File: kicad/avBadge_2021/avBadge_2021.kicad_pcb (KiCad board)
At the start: 2 copper layers, 115 x 75 mm, 36 parts, among them J1 AVR-ISP-6, Q1 2N3904, SW1 SW_Push_Dual, SW2 SW_SPDT, U1 ATtiny84A-SSU

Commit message: arduino code updates and manufactured v01 gerbers completed.
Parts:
- Q1: footprint TO_SOT_Packages_SMD:SOT-23 -> aerospace_badge:SOT-23-NPN

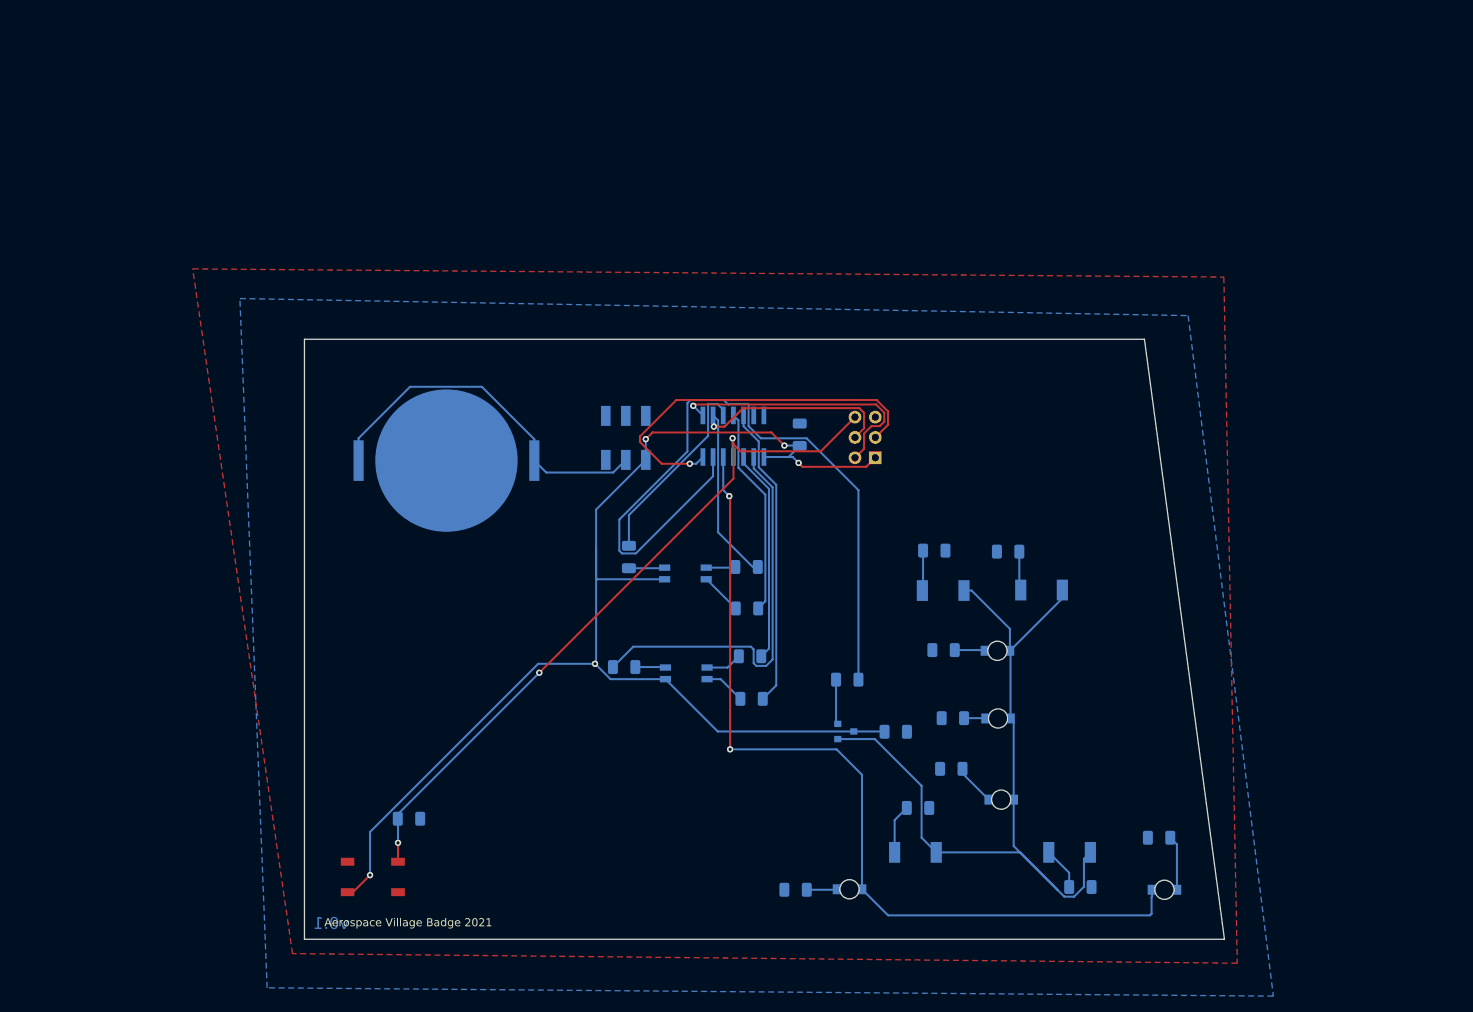
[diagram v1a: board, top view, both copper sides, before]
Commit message: refactor of kicad files working through incorporation of art and new MCU design.
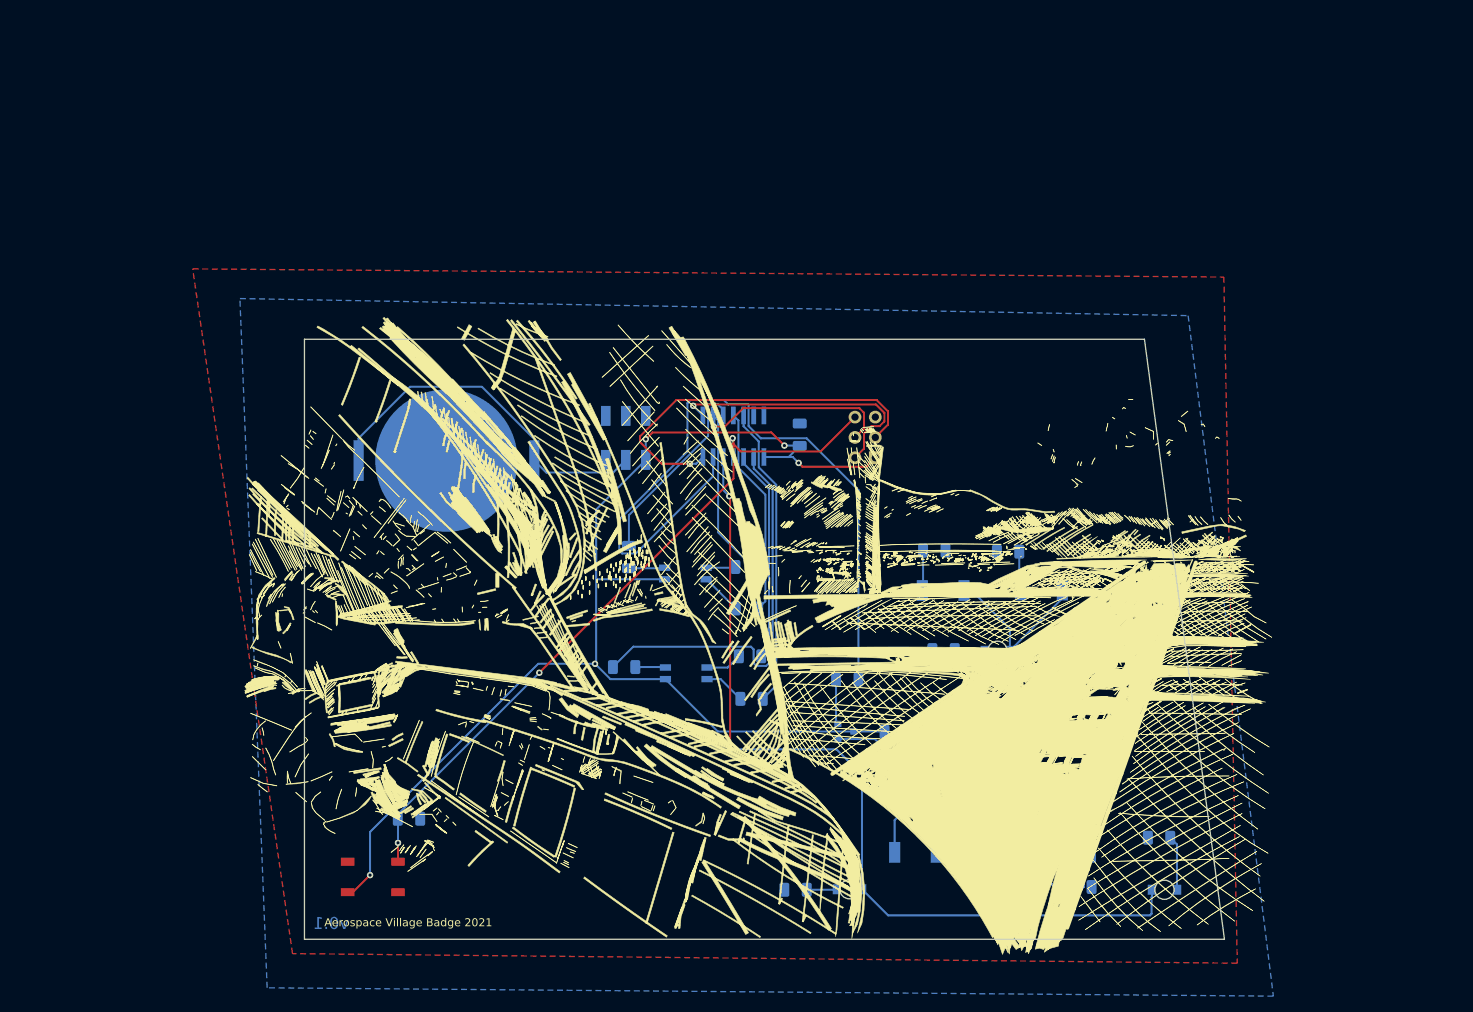
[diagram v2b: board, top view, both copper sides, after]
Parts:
- added svg2mod: G***, aerospace_badge:test, F.Cu at (142.1, 102.9)

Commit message: v0.2 gerber builtout and sent for fabrication.
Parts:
- removed the D5 at (171.4, 134.1)
- removed the SW1 at (103.5, 137.2)
- removed svg2mod: G***, aerospace_badge:test
- added D12: LED, sunled:XZMYK45WT-9, B.Cu at (185.3, 117.4)
- added D4: LED, sunled:XZDGK45WT-9, B.Cu at (205.2, 81.1)
- added P1: SerialConnector, aerospace_badge:serialConnector, B.Cu at (116.6, 114.2)
- added R11: 330, Resistors_SMD:R_1206_3216Metric, B.Cu at (198.5, 81.1)
- added R12: 10K, Resistors_SMD:R_1206_3216Metric, B.Cu at (137.5, 125.0)
- added R7: 10K, Resistors_SMD:R_1206_3216Metric, B.Cu at (129.1, 120.2)
- added S1: OpenConnections, aerospace_badge:artboard, F.Cu at (150.5, 104.7)
- added VR1: TLV702, TO_SOT_Packages_SMD:SOT-23-5, B.Cu at (110.0, 95.4)
- BT1: footprint Battery:BatteryHolder_Keystone_3034_1x20mm -> aerospace_badge:BHX2-2032
- D1, D2: value APFA3010 -> SunLED_RGB_ReverseMount
- D10, D11: footprint aerospace_badge:led_in-s124ar -> sunled:XZMYK45WT-9
- D6: footprint sunled:XZDGK45WT-9 -> sunled:XZM2CRK45WT-9
- D8: footprint sunled:XZM2CRK45WT-9 -> sunled:XZDGK45WT-9
- D9: footprint aerospace_badge:led_in-s124ar -> sunled:XZDGK45WT-9
- J1: moved to F.Cu
- U1: value ATtiny84A-SSU -> ATmega8-16AU; footprint aerospace_badge:attiny84 -> digikey-footprints:TQFP-32_7x7mm
- moved J1 68.6 mm to (95.2, 86.9), turned to 45 degrees
- moved C1 47.7 mm to (113.6, 101.9)
- moved D1 40.1 mm to (165.4, 78.7)
- moved R2 35.1 mm to (172.6, 87.3)
- moved R4 34.6 mm to (157.0, 84.3)
- moved U1 33.5 mm to (124.3, 105.2), turned to 0 degrees
- moved R6 33.4 mm to (172.6, 84.3)
- moved R1 32.2 mm to (172.5, 80.4)
- moved R5 30.4 mm to (172.2, 77.4)
- moved R3 29.3 mm to (157.6, 77.9), turned to 0 degrees
- moved D7 29.1 mm to (188.9, 126.8)
- moved R9 28.8 mm to (135.1, 120.1)
- moved D11 28.4 mm to (197.3, 103.5), turned to 180 degrees
- moved D9 27.6 mm to (206.4, 96.8), turned to 270 degrees
- moved R19 27.3 mm to (201.6, 107.6), turned to 0 degrees
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- renumbered D4 to D5, R2 to R1, R8 to R10, R10 to R13, R11 to R14, R12 to R15, R13 to R16, R14 to R17, R15 to R18, R16 to R19, R1 to R2, R17 to R20, R4 to R3, R3 to R4, R6 to R5, R5 to R6, R7 to R8, SW2 to SW1
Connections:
- R1 pad 1: Net-(R2-Pad1) -> Net-(R1-Pad1)
- R1 pad 2: Net-(D2-Pad1) -> Net-(D1-Pad1)
- R13 pad 2: Net-(R10-Pad2) -> Net-(R13-Pad2)
- R14 pad 1: Net-(D5-Pad1) (its old number) -> Net-(D6-Pad1)
- R15 pad 1: Net-(D6-Pad1) -> Net-(D7-Pad1)
- R16 pad 1: Net-(D7-Pad1) -> Net-(D8-Pad1)
- R17 pad 1: Net-(D8-Pad1) -> Net-(D9-Pad1)
- R18 pad 1: Net-(D9-Pad1) -> Net-(D10-Pad1)
- R19 pad 1: Net-(D10-Pad1) -> Net-(D11-Pad1)
- R2 pad 1: Net-(R1-Pad1) -> Net-(R2-Pad1)
- R2 pad 2: Net-(D1-Pad1) -> Net-(D2-Pad1)
- R20 pad 1: Net-(D11-Pad1) -> Net-(D12-Pad1)
- R3 pad 1: Net-(R4-Pad1) -> Net-(R3-Pad1)
- R3 pad 2: Net-(D2-Pad3) -> Net-(D1-Pad3)
- R4 pad 1: Net-(R3-Pad1) -> Net-(R4-Pad1)
- R4 pad 2: Net-(D1-Pad3) -> Net-(D2-Pad3)
- R5 pad 1: Net-(J1-Pad3) -> Net-(R5-Pad1)
- R5 pad 2: Net-(D2-Pad4) -> Net-(D1-Pad4)
- R6 pad 1: Net-(R5-Pad1) -> Net-(R6-Pad1)
- R6 pad 2: Net-(D1-Pad4) -> Net-(D2-Pad4)
- R9 pad 2: Net-(J1-Pad5) -> Net-(R9-Pad2)
- SW1 pad 1: VCC -> Net-(SW1-Pad1)
- U1 pad 1: VCC -> Net-(R12-Pad2)
- U1 pad 11: Net-(R2-Pad1) -> Net-(U1-Pad11)
- U1 pad 12: Net-(R1-Pad1) -> Net-(D4-Pad2)
- U1 pad 13: Net-(U1-Pad13) -> Net-(R6-Pad1)
- U1 pad 14: GND -> Net-(R13-Pad2)
- U1 pad 2: Net-(R3-Pad1) -> Net-(R7-Pad2)
- U1 pad 3: Net-(R5-Pad1) -> GND
- U1 pad 4: Net-(J1-Pad5) -> VCC
- U1 pad 5: Net-(D3-Pad2) -> GND
- U1 pad 6: Net-(R10-Pad2) -> VCC
- U1 pad 7: Net-(J1-Pad4) -> Net-(U1-Pad7)
- U1 pad 8: Net-(J1-Pad1) -> Net-(U1-Pad8)
- U1 pad 9: Net-(J1-Pad3) -> Net-(R2-Pad1)
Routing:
- net GND: track 0.00 -> 128.6 mm, vias 0 -> 6
- net Net-(D4-Pad2): track 0.00 -> 95.6 mm, vias 0 -> 2
- net Net-(R10-Pad2): track 91.8 -> 0.00 mm
- net VCC: track 166.1 -> 257.8 mm, vias 5 -> 2
- net Net-(R6-Pad1): track 0.00 -> 85.8 mm, vias 0 -> 2
- net Net-(SW1-Pad1): track 0.00 -> 65.1 mm
- net Net-(R3-Pad1): track 50.4 -> 114.3 mm, vias 0 -> 3
- net Net-(R13-Pad2): track 0.00 -> 53.7 mm, vias 0 -> 2
- net Net-(R5-Pad1): track 26.6 -> 79.2 mm
- net Net-(J1-Pad5): track 90.1 -> 38.3 mm, vias 3 -> 1
- net Net-(R2-Pad1): track 26.2 -> 63.4 mm, vias 0 -> 2
- net Net-(R1-Pad1): track 38.4 -> 73.3 mm
- net Net-(R9-Pad2): track 0.00 -> 34.6 mm, vias 0 -> 2
- net Net-(R12-Pad2): track 0.00 -> 34.2 mm, vias 0 -> 2
- net Net-(R7-Pad2): track 0.00 -> 32.6 mm, vias 0 -> 1
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- added copper zone on F.Cu, net GND
- removed copper zone on F.Cu, net VCC
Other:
- board size 115 x 75 mm -> 127 x 78 mm
- rule pad_to_mask_clearance: 0.05 -> 0
- board text added: "v0.2"
- board text removed: "v0.1"

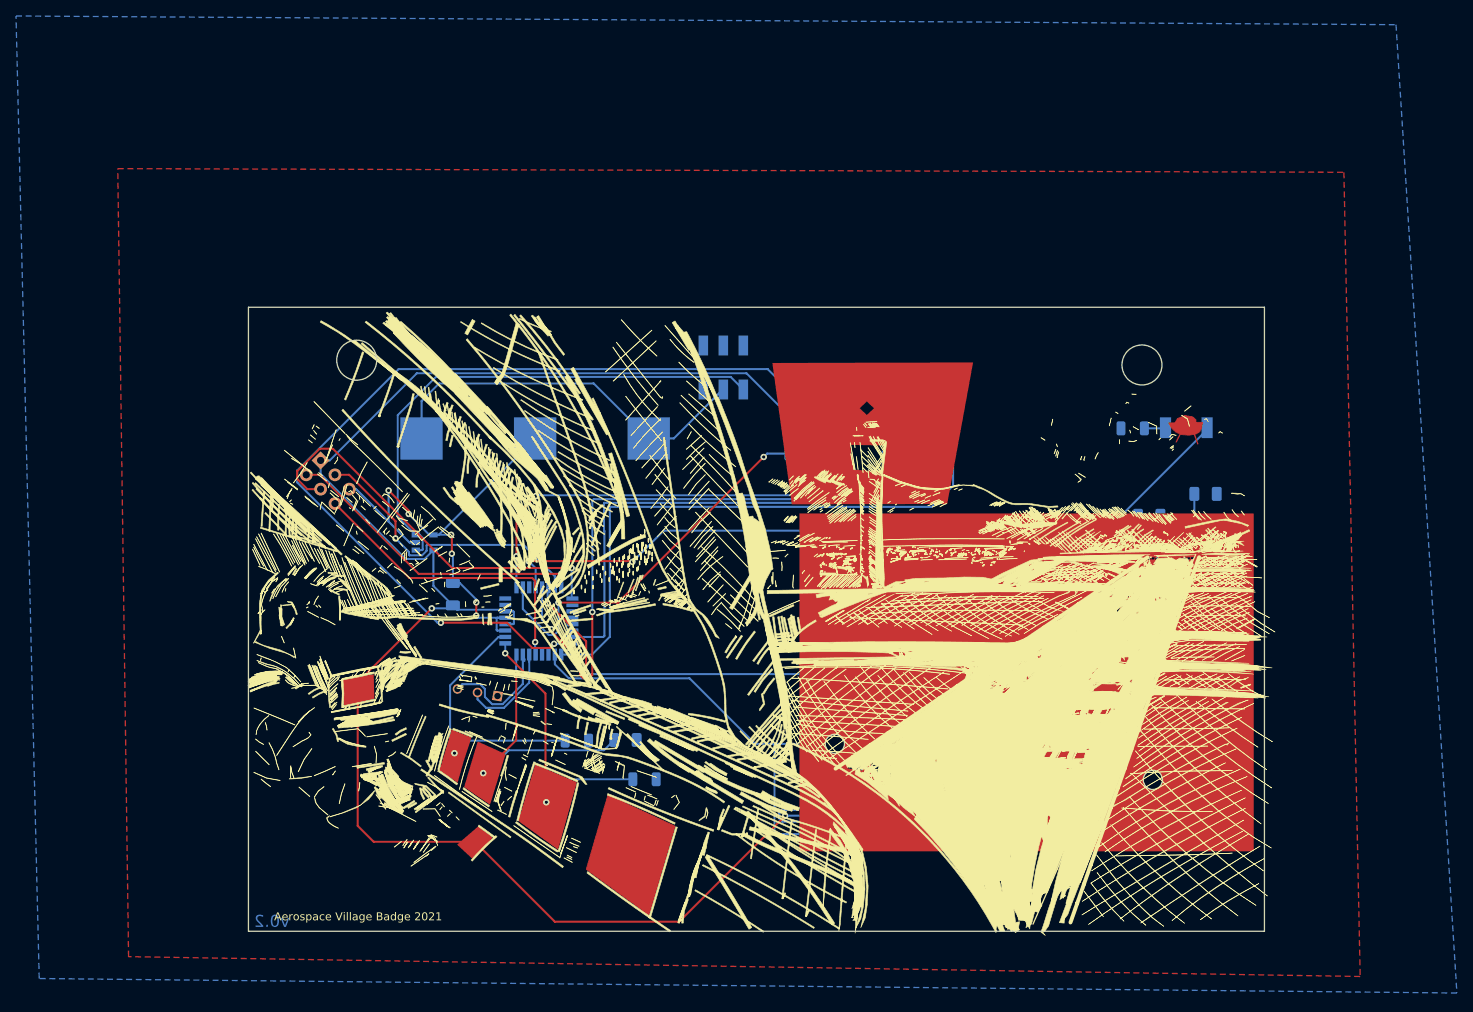
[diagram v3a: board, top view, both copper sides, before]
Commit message: incremental improvements to art, edgecuts, layout
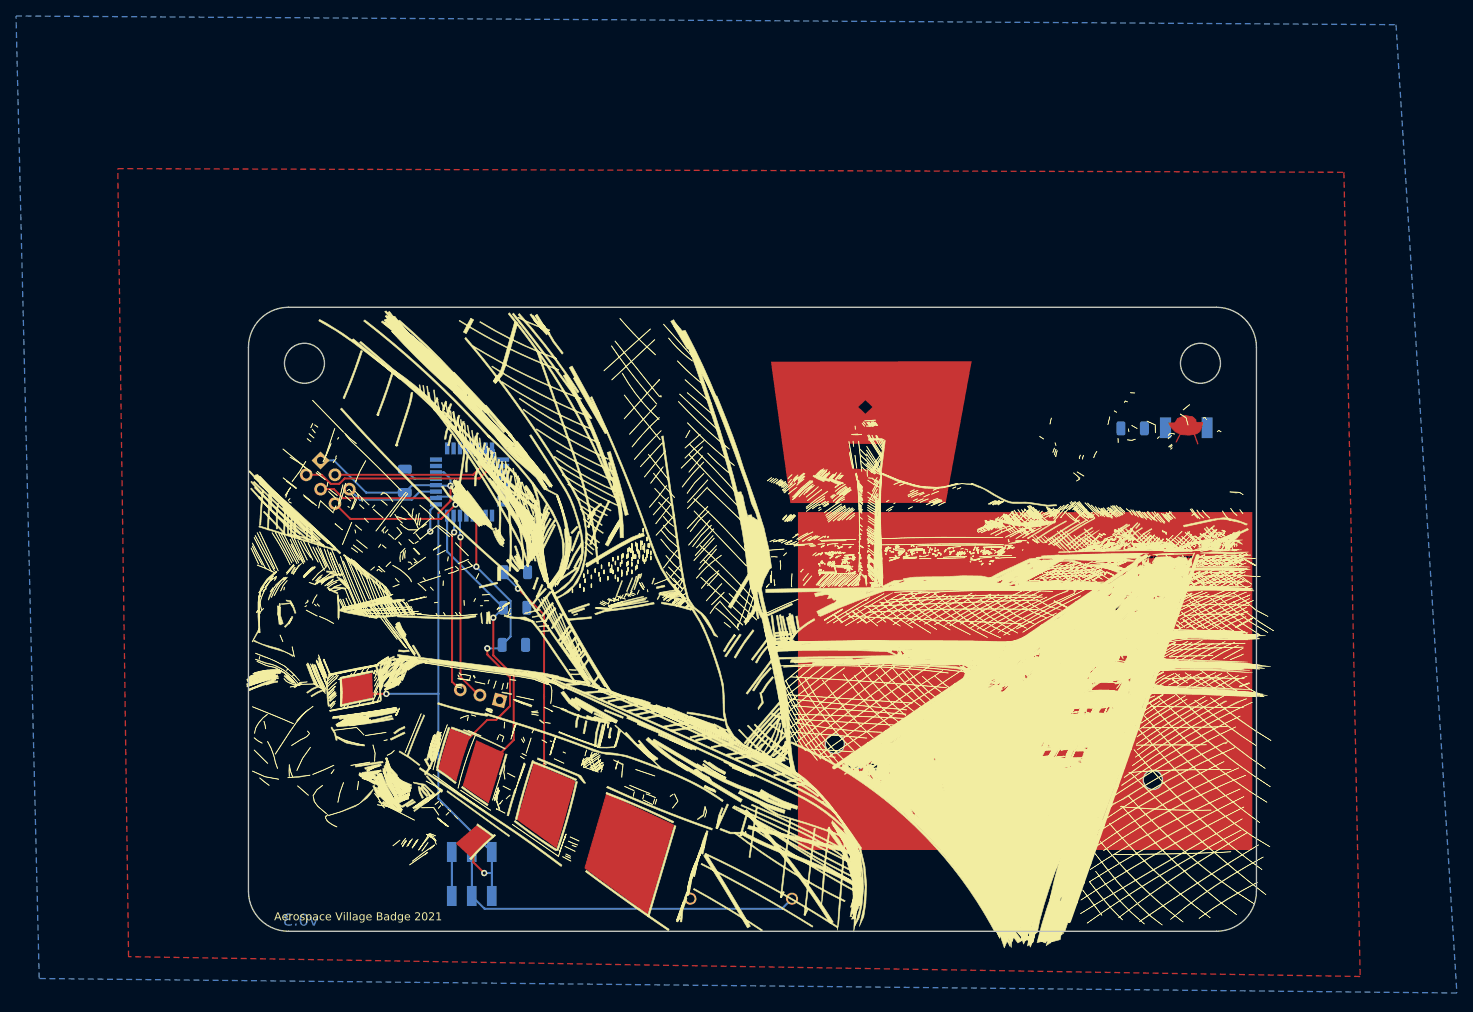
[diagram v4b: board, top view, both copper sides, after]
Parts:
- removed D9: LED, sunled:XZDGK45WT-9
- removed R17: 330, Resistors_SMD:R_1206_3216Metric
- removed VR1: TLV702, TO_SOT_Packages_SMD:SOT-23-5
- BT1: footprint aerospace_badge:BHX2-2032 -> 2479_battery_holder:2479
- moved SW1 70.7 mm to (115.9, 136.8)
- moved BT1 40.4 mm to (144.9, 116.8), turned to 270 degrees
- moved R12 30.5 mm to (121.4, 99.1)
- moved D6 21.7 mm to (189.5, 123.9)
- moved D7 21.7 mm to (167.5, 123.7)
- moved R9 21.5 mm to (121.3, 103.6)
- moved R15 20.3 mm to (167.7, 127.9)
- moved R14 19.5 mm to (182.9, 124.5)
- moved U1 19.4 mm to (115.6, 87.8)
- moved R19 15.9 mm to (187.9, 99.5)
- moved C1 15.4 mm to (107.5, 87.7)
- moved R7 14.3 mm to (121.2, 108.2)
- moved R18 9.83 mm to (186.8, 107.4)
- moved D12 9.12 mm to (193.7, 113.7), turned to 0 degrees
- moved R16 8.29 mm to (192.4, 93.4), turned to 0 degrees
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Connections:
- SW1 pad 1: Net-(SW1-Pad1) -> VCC
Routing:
- net VCC: track 257.8 -> 92.1 mm, vias 2 -> 3
- net Net-(R3-Pad1): track 114.3 -> 0.00 mm, vias 3 -> 0
- net GND: track 128.6 -> 16.2 mm, vias 6 -> 0
- net Net-(D3-Pad2): track 98.7 -> 0.00 mm
- net Net-(D4-Pad2): track 95.6 -> 0.00 mm, vias 2 -> 0
- net Net-(R6-Pad1): track 85.8 -> 0.00 mm, vias 2 -> 0
- net Net-(R5-Pad1): track 79.2 -> 0.00 mm
- net Net-(R1-Pad1): track 73.3 -> 0.00 mm
- net Net-(D10-Pad2): track 71.7 -> 0.00 mm
- net Net-(SW1-Pad1): track 65.1 -> 0.00 mm
- net Net-(R2-Pad1): track 63.4 -> 0.00 mm, vias 2 -> 0
- net Net-(R13-Pad2): track 53.7 -> 0.00 mm, vias 2 -> 0
- net Net-(R4-Pad1): track 49.7 -> 0.00 mm, vias 2 -> 0
- net Net-(J1-Pad3): track 49.9 -> 14.2 mm, vias 1 -> 0
- net Net-(J1-Pad5): track 38.3 -> 19.0 mm
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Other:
- board size 127 x 78 mm -> 126 x 78 mm
- board text added: "v0.3"
- board text removed: "v0.2"

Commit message: artwork cleanup and general tweaks. Incremental save.
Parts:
- added QR*****: qrc, aerospace_badge:qrc, B.Cu at (99.5, 132.8)
- D4: footprint sunled:XZDGK45WT-9 -> sunled:XZFBB45S-9
- S1: footprint aerospace_badge:artboard -> aerospace_badge:artboard2
- moved P1 41.5 mm to (92.3, 81.1), turned to 75 degrees
- moved S1 3.22 mm to (147.1, 104.3)
- moved SW1 0.08 mm to (116.0, 136.9), turned to 270 degrees
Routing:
- net Net-(P1-Pad2): track 23.6 -> 2.72 mm
- net Net-(P1-Pad1): track 22.4 -> 2.49 mm
- net Net-(R9-Pad2): track 40.0 -> 24.7 mm
- net Net-(R12-Pad2): track 34.8 -> 21.5 mm
- net VCC: track 92.1 -> 80.6 mm
- net Net-(J1-Pad3): track 14.2 -> 3.41 mm
- net Net-(R7-Pad2): track 44.8 -> 41.8 mm
- net Net-(BT1-Pad1): track 46.7 -> 45.2 mm
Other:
- board text added: "ISP"
